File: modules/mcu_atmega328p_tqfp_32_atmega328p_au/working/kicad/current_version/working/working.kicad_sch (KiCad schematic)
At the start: 2 parts, among them U1 itq32at328

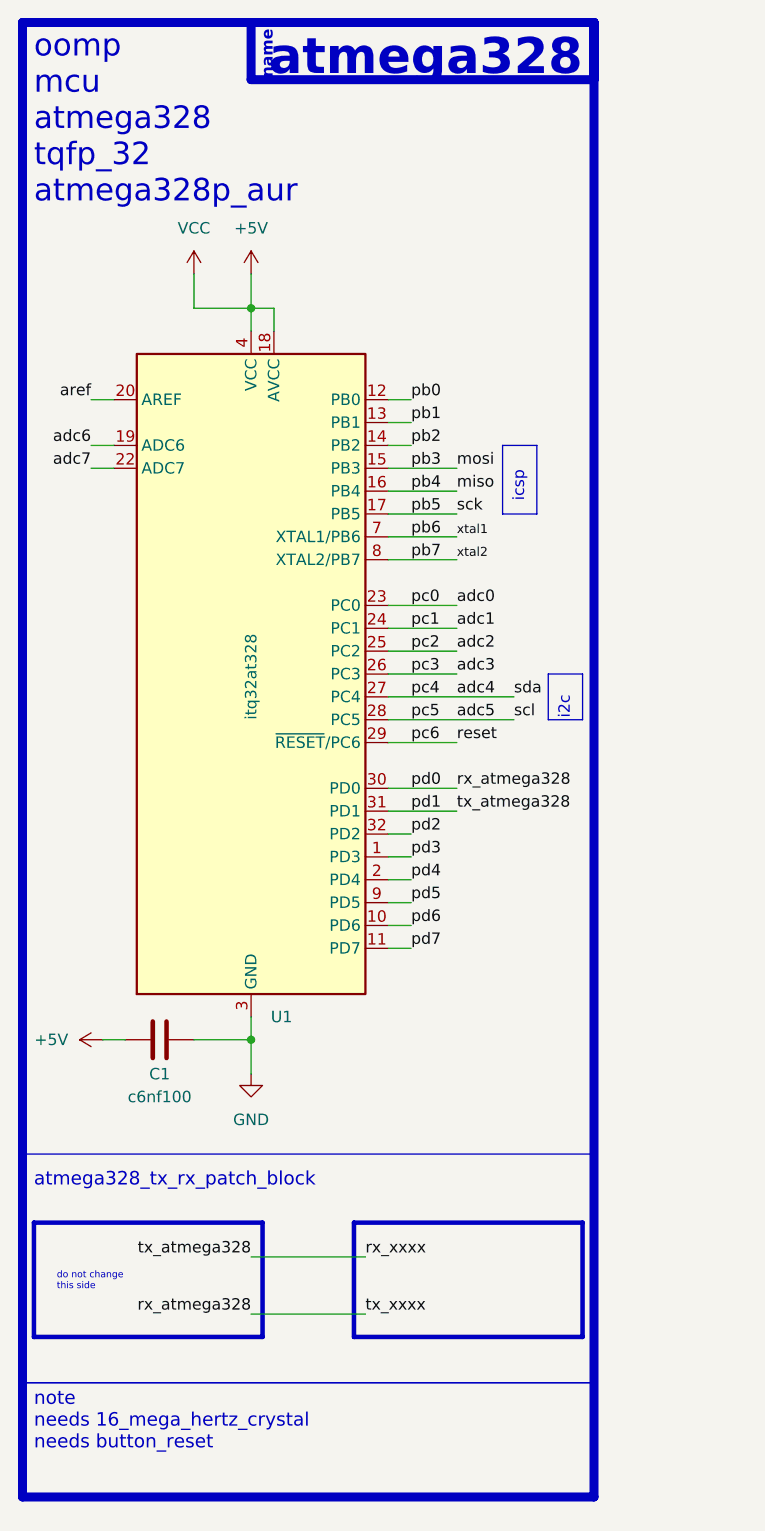
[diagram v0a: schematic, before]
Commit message: fixed formatting to be more consistent
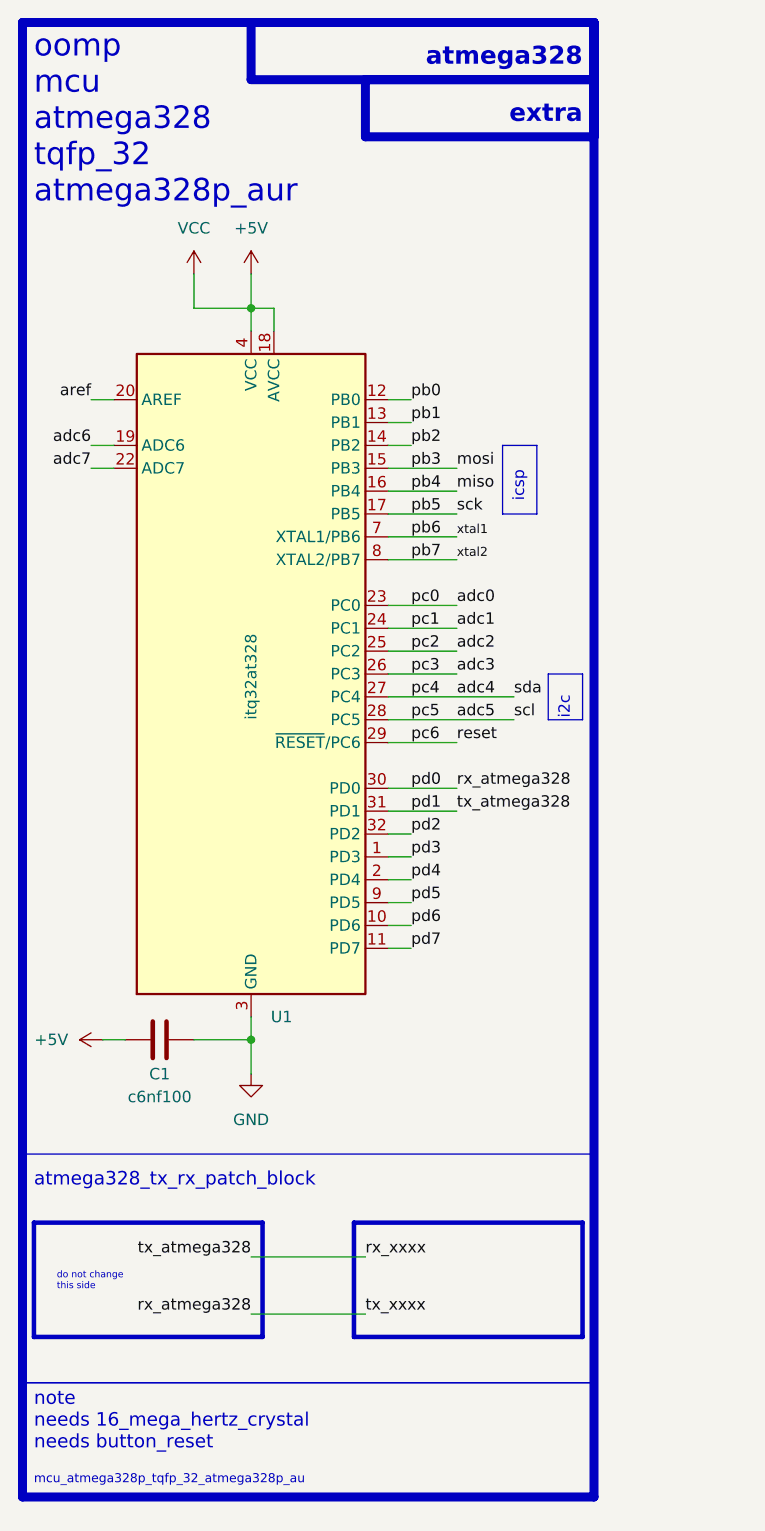
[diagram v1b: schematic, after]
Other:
- note added: "extra"
- note added: "mcu_atmega328p_tqfp_32_atmega328p_au"
- note removed: "name"
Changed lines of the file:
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@@
   (rectangle (start 119.38 17.78) (end 157.48 24.13)
     (stroke (width 1) (type default))
-    (fill (type color) (color 0 0 0 0))
+    (fill (type none))
   )
   (rectangle (start 95.25 151.13) (end 120.65 163.83)
@@
   (rectangle (start 147.32 64.77) (end 151.13 72.39)
     (stroke (width 0) (type default))
+    (fill (type none))
+  )
+  (rectangle (start 132.08 24.13) (end 157.48 30.48)
+    (stroke (width 1) (type default))
     (fill (type none))
   )
@@
     (effects (font (size 1.27 1.27)) (justify left bottom))
   )
-  (text "atmega328" (at 156.21 24.13 0)
-    (effects (font (size 4 4) (thickness 0.8) bold (color 255 255 255 1)) (justify right bottom))
-  )
-  (text "name" (at 121.92 24.13 90)
-    (effects (font (size 1.27 1.27) (thickness 0.254) bold (color 255 255 255 1)) (justify left bottom))
+  (text "atmega328" (at 156.21 22.86 0)
+    (effects (font (size 2 2) (thickness 0.8) bold) (justify right bottom))
   )
   (text "note\nneeds 16_mega_hertz_crystal\nneeds button_reset\n"
@@
     (effects (font (size 2.5 2.5)) (justify left bottom))
   )
+  (text "mcu_atmega328p_tqfp_32_atmega328p_au" (at 95.25 180.34 0)
+    (effects (font (size 1 1)) (justify left bottom))
+  )
   (text "atmega328_tx_rx_patch_block" (at 95.25 147.32 0)
     (effects (font (size 1.5 1.5)) (justify left bottom))
   )
+  (text "extra" (at 156.21 29.21 0)
+    (effects (font (size 2 2) (thickness 0.8) bold) (justify right bottom))
+  )
   (text "do not change\nthis side" (at 97.79 158.75 0)

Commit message: schematic formatting
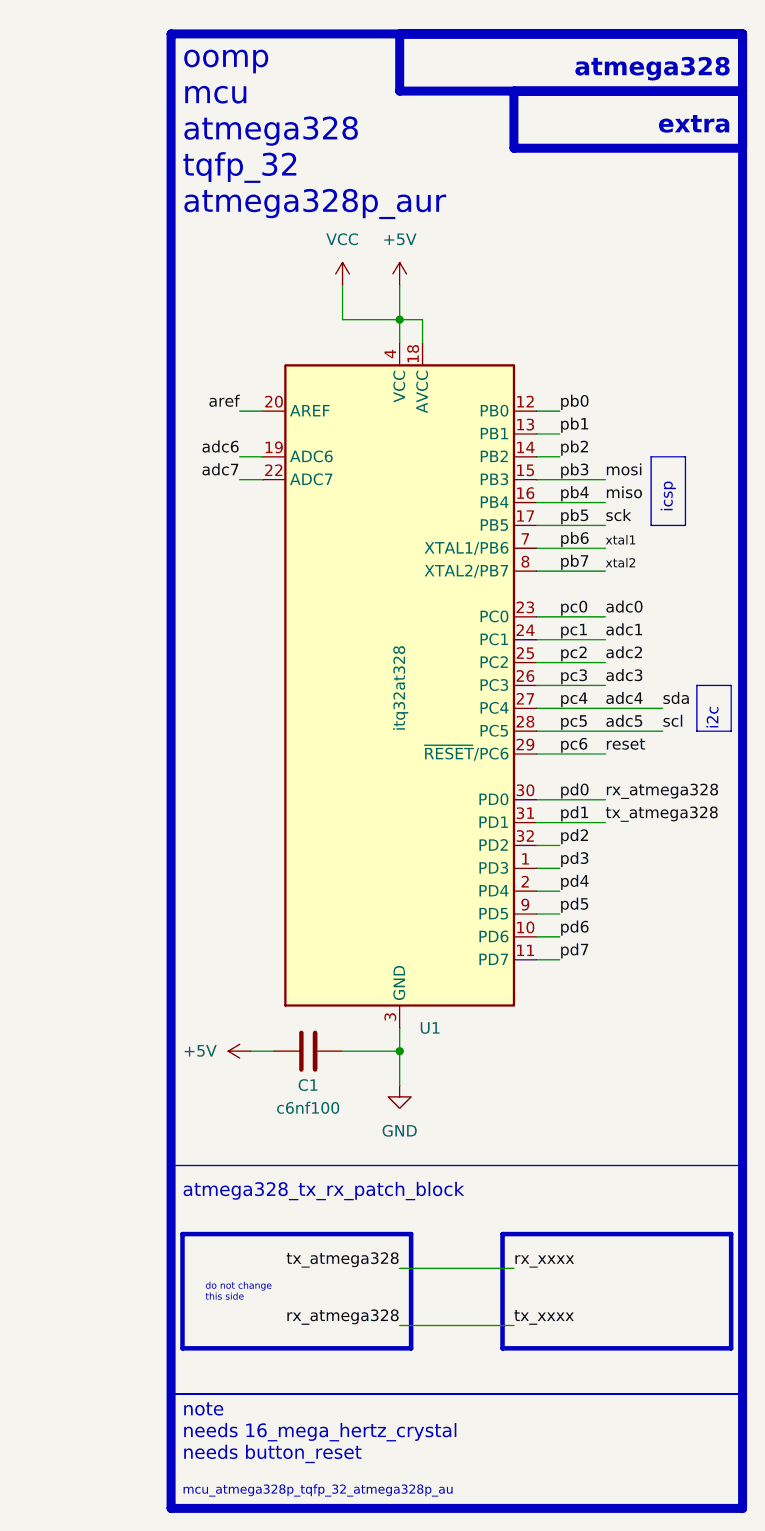
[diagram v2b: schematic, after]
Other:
- moved on the sheet: C1, U1
